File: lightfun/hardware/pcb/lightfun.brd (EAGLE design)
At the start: 23 x 38 mm, 10 parts, among them J1 FIRMWARE, P1 ESP8266, P2 ESP8266 CONNECTOR, P3 +5V GND, P4 TX RX, P5 GND, P6 +5V GND IO0 IO2, T1 LM2937ET

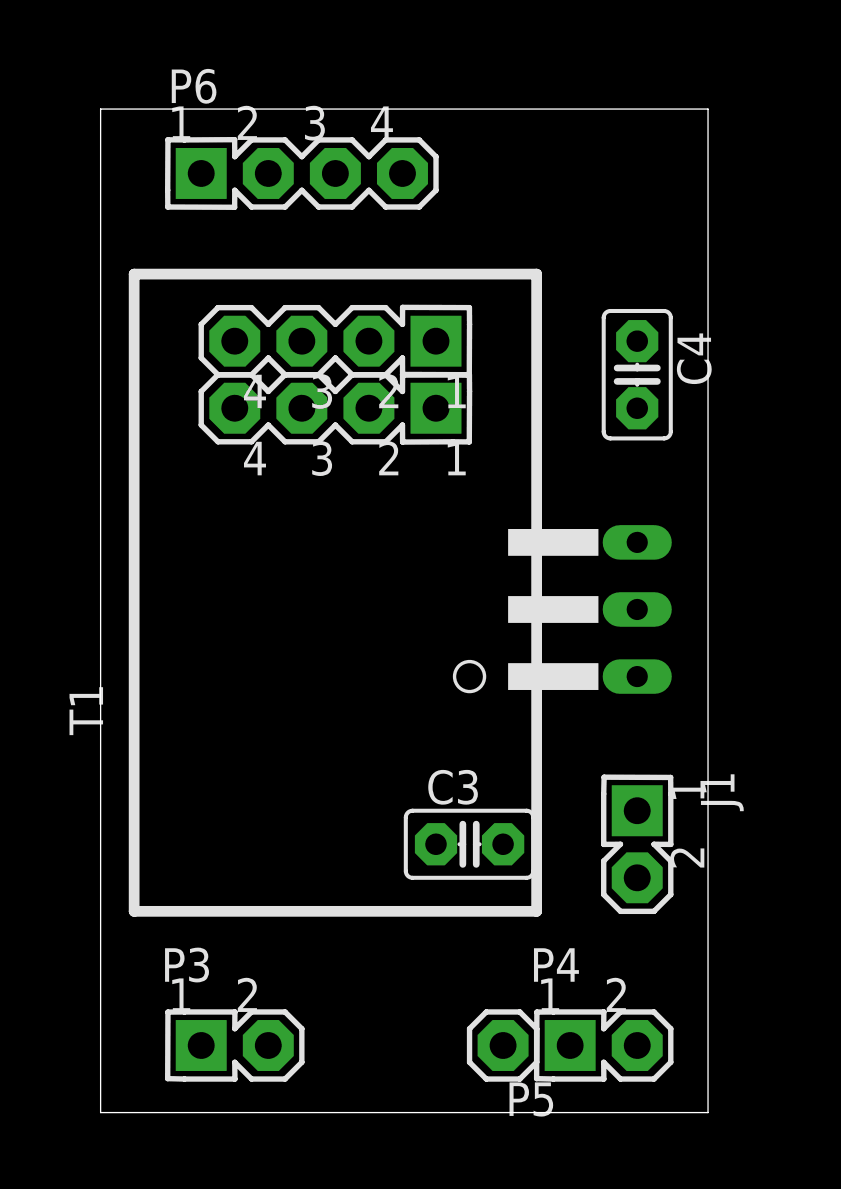
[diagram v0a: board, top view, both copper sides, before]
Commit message: Generic ESP8266 PCB routing
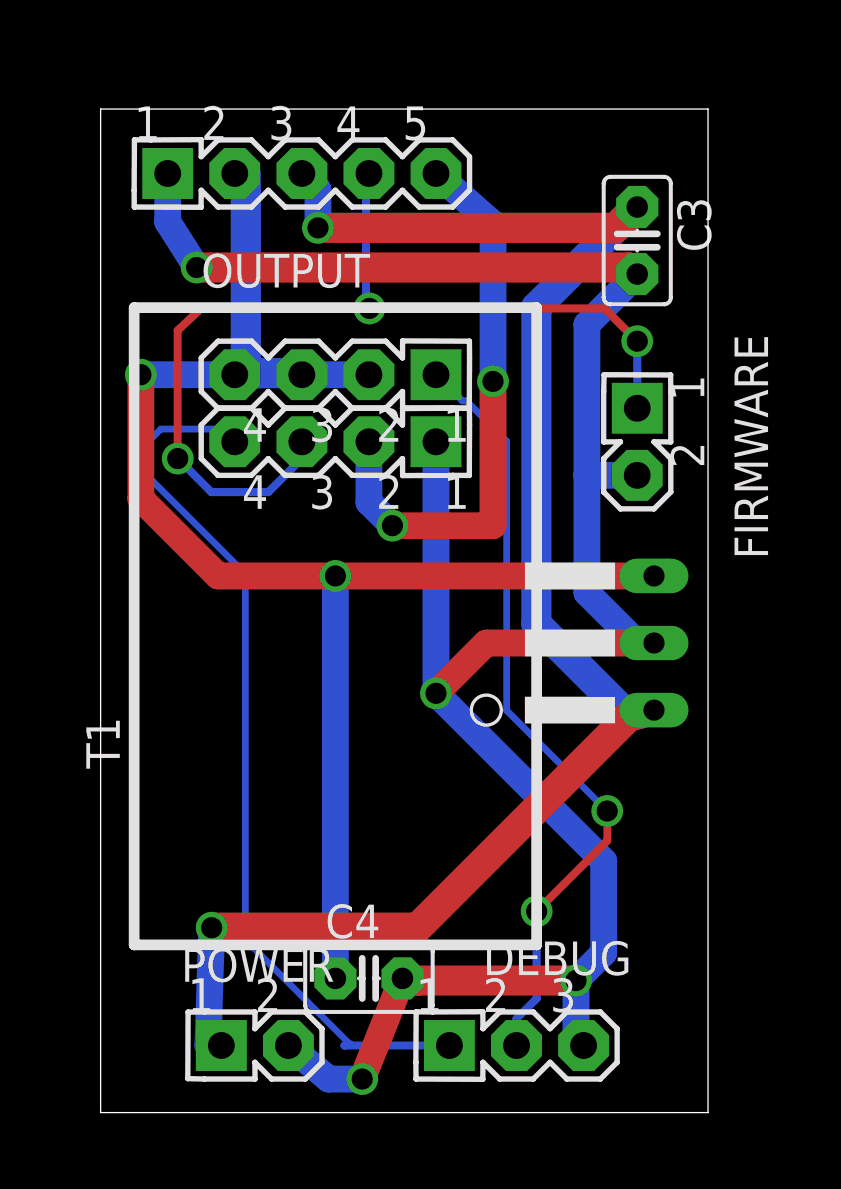
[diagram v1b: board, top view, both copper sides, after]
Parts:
- removed J1: FIRMWARE, stutz-eagle:PIN-HEADER-2PIN
- removed P3: +5V GND, stutz-eagle:PIN-HEADER-2PIN
- removed P4: TX RX, stutz-eagle:PIN-HEADER-2PIN
- removed P5: GND, stutz-eagle:PIN-HEADER-1PIN
- removed P6: +5V GND IO0 IO2, stutz-eagle:PIN-HEADER-4PIN
- added DEBUG: RX TX GND, stutz-eagle:PIN-HEADER-3PIN
- added FIRMWARE: FIRMWARE, stutz-eagle:PIN-HEADER-2PIN
- added OUTPUT: GND 3.3V 5V IO0 IO2, stutz-eagle:PIN-HEADER-5PIN
- added POWER: +5V GND, stutz-eagle:PIN-HEADER-2PIN
- moved C4 25.0 mm to (10.2, 5.08), turned to 0 degrees
- moved C3 23.7 mm to (20.3, 33.0), turned to 270 degrees
- moved T1 1.42 mm to (12.1, 17.8)
- moved P2 1.27 mm to (8.89, 25.4)
- moved P1 1.27 mm to (8.89, 27.9)
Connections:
- net +3.3V: now also OUTPUT.2
- net +5V: now also OUTPUT.3, POWER.1; no longer P3.1, P6.1
- net ESP_GPIO0: now also FIRMWARE.1, OUTPUT.4; no longer J1.1, P6.3
- net ESP_GPIO2: now also OUTPUT.5; no longer P6.4
- net ESP_RX: now also DEBUG.1; no longer P4.1
- net ESP_TX: now also DEBUG.2; no longer P4.2
- net GND: now also DEBUG.3, FIRMWARE.2, OUTPUT.1, POWER.2; no longer J1.2, P3.2, P5.1, P6.2
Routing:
- net GND: track 0.00 -> 87.9 mm, vias 0 -> 4
- net +5V: track 0.00 -> 63.1 mm, vias 0 -> 2
- net +3.3V: track 0.00 -> 57.6 mm, vias 0 -> 2
- net ESP_GPIO0: track 0.00 -> 37.2 mm, vias 0 -> 3
- net ESP_RX: track 0.00 -> 33.8 mm
- net ESP_TX: track 0.00 -> 29.6 mm, vias 0 -> 2
- net ESP_GPIO2: track 0.00 -> 21.7 mm, vias 0 -> 2
